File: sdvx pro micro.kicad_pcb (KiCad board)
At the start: 2 copper layers, 124 x 44 mm, 15 parts

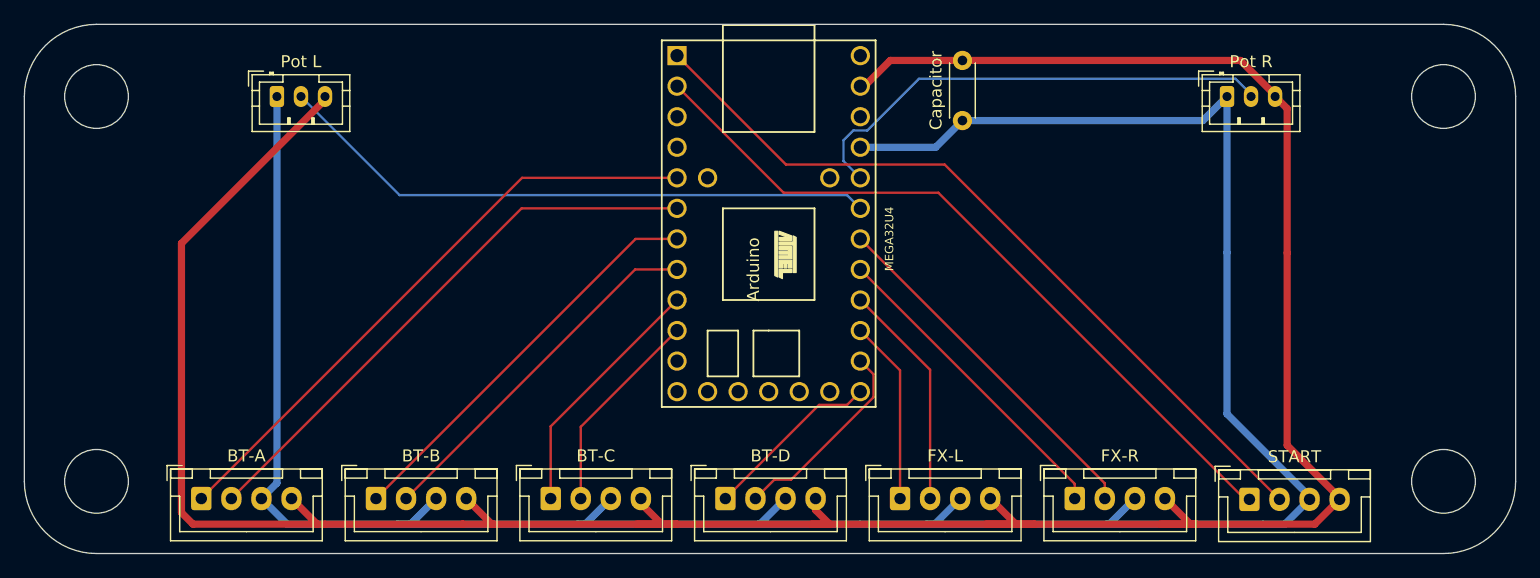
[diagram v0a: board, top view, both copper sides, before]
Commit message: Redesigned for Raspberry Pi Pico
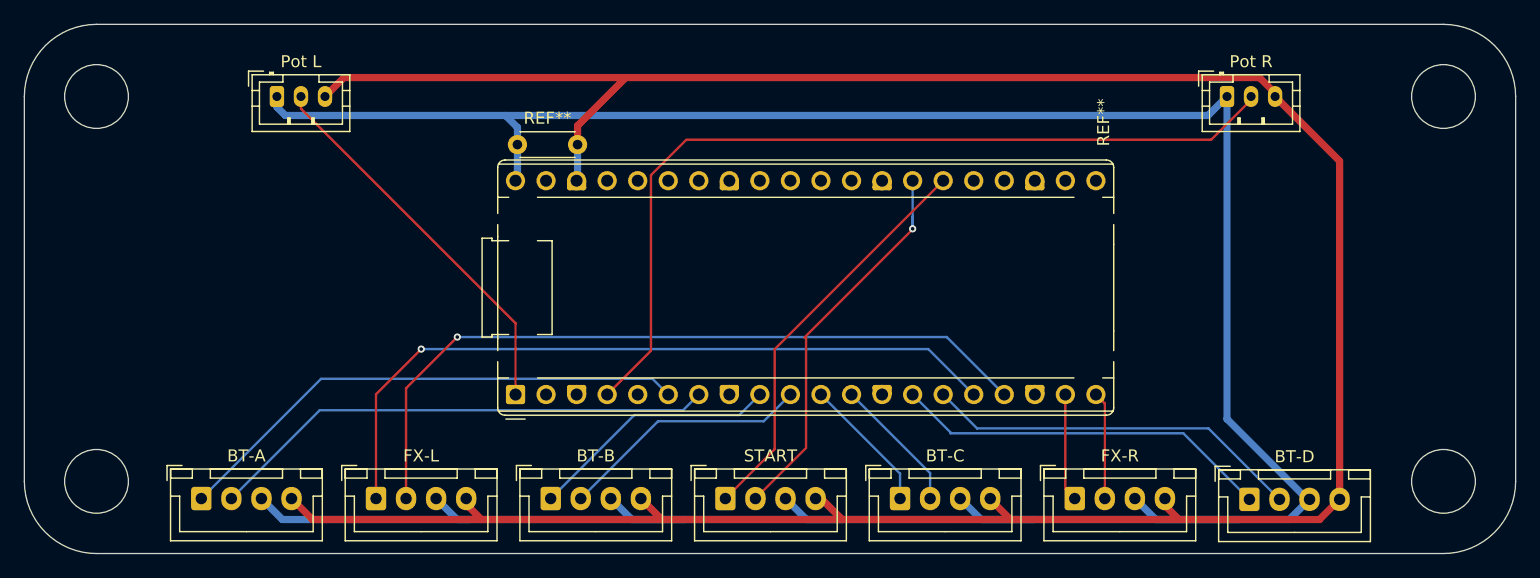
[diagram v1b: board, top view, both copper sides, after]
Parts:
- removed Arduino: Teensy2.0, teensy:Teensy2.0
- removed Capacitor: C_Disc_D4.3mm_W1.9mm_P5.00mm, Capacitor_THT:C_Disc_D4.3mm_W1.9mm_P5.00mm
- added REF**: C_Disc_D4.3mm_W1.9mm_P5.00mm, Capacitor_THT:C_Disc_D4.3mm_W1.9mm_P5.00mm, F.Cu at (35.0, 4.00)
- added REF**: RaspberryPi_Pico_Common_THT, Module:RaspberryPi_Pico_Common_THT, F.Cu at (34.8, 24.8)
- renumbered BT-C to BT-B, FX-L to BT-C, START to BT-D, BT-B to FX-L, BT-D to START
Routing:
- net 5V: track 210.0 -> 243.9 mm
- net LightData: track 225.8 -> 210.9 mm, vias 0 -> 2
- net EncData: track 90.8 -> 104.7 mm
- net Ground: track 239.6 -> 227.3 mm
- net ButtonData: track 223.9 -> 211.9 mm, vias 0 -> 1
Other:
- board text added: "Minnowboard V3"
- board text added: "Pi Pico"
- board text removed: "Minnowboard V2"
- board text removed: "Pro Micro goes here ->"
